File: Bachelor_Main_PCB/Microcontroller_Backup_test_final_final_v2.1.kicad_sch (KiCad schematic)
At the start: 68 parts, among them J13 Conn_01x07_Pin, J14 M20-9990245, J15 M20-9990245, J17 MEM2075-00-140-01-A, Q3 SSM3J358R,LF, U3 STM32H7A3ZITxQ, U4 USB3320C-EZK-TR, U7 ESD7004MUTAG, U8 ESD7004MUTAG, Y4 SG-210STF 24Mhz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

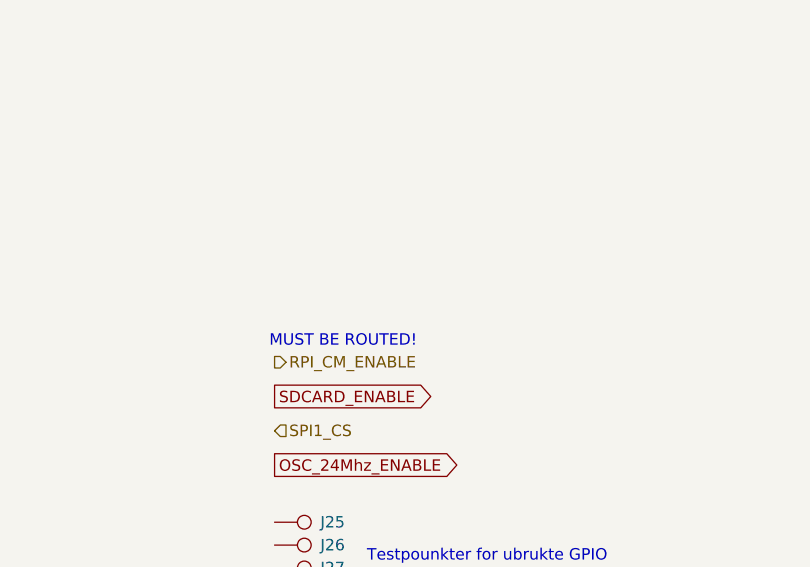
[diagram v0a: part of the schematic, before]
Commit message: Removed Modem_safe_PWR_remove pin.
was potential use for the MCU but would require level shifters and would not add any functionality ass the RPI controls the Modem anyway.
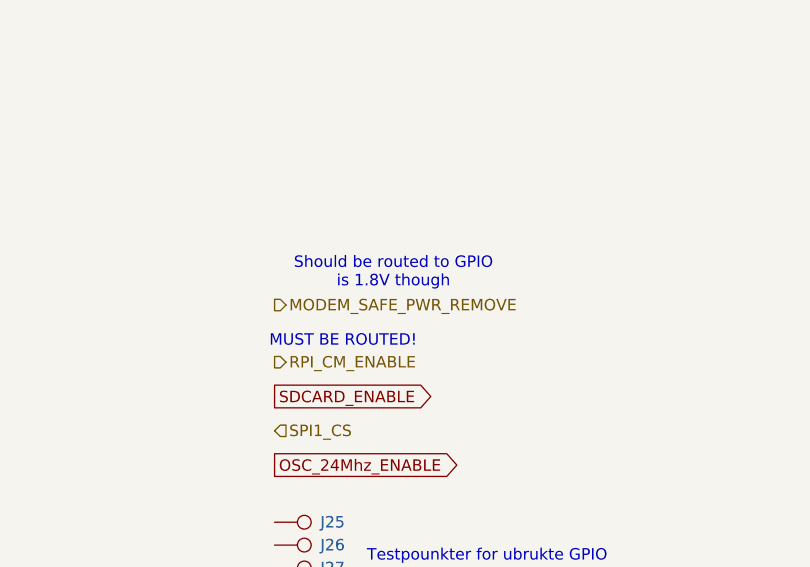
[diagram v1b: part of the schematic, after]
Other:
- note added: "Should be routed to GPIO is 1.8V though"
